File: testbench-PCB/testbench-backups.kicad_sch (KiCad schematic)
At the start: 16 parts, among them J2 AVR-ISP-6, SW1 RESET, U1 ATmega2561-16A, U5 ATmega328P_Xplained_Mini, Y1 X322516MLB4SI

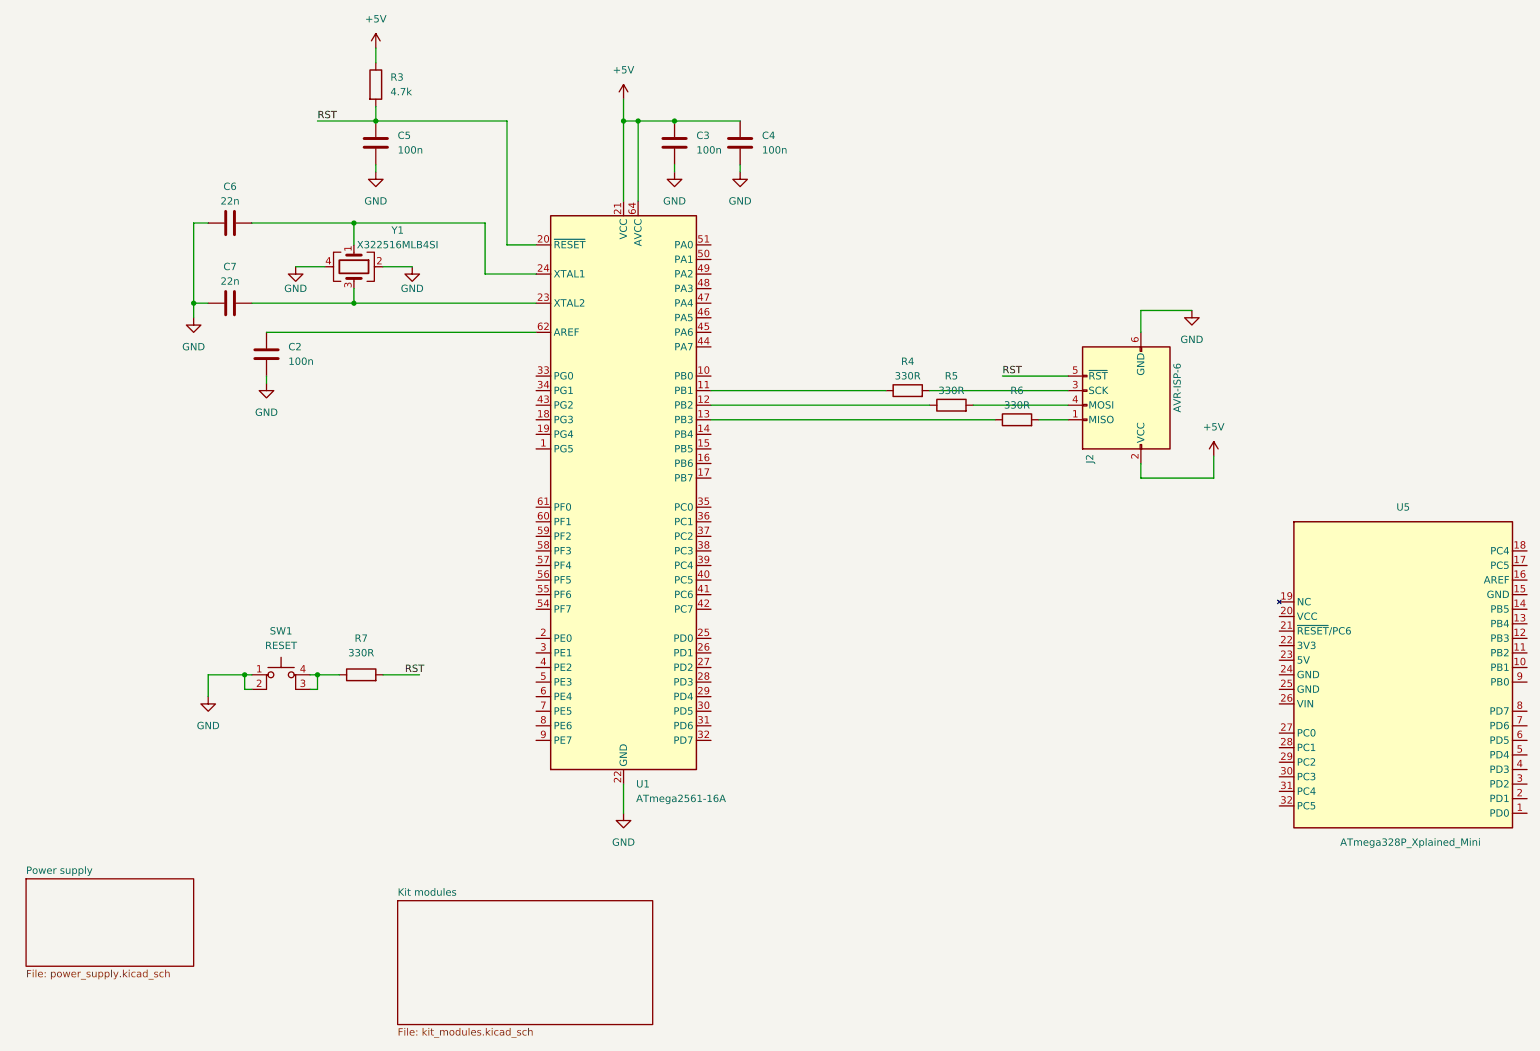
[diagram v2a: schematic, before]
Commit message: Changed USB interface name, MCU moved to separate sheet.
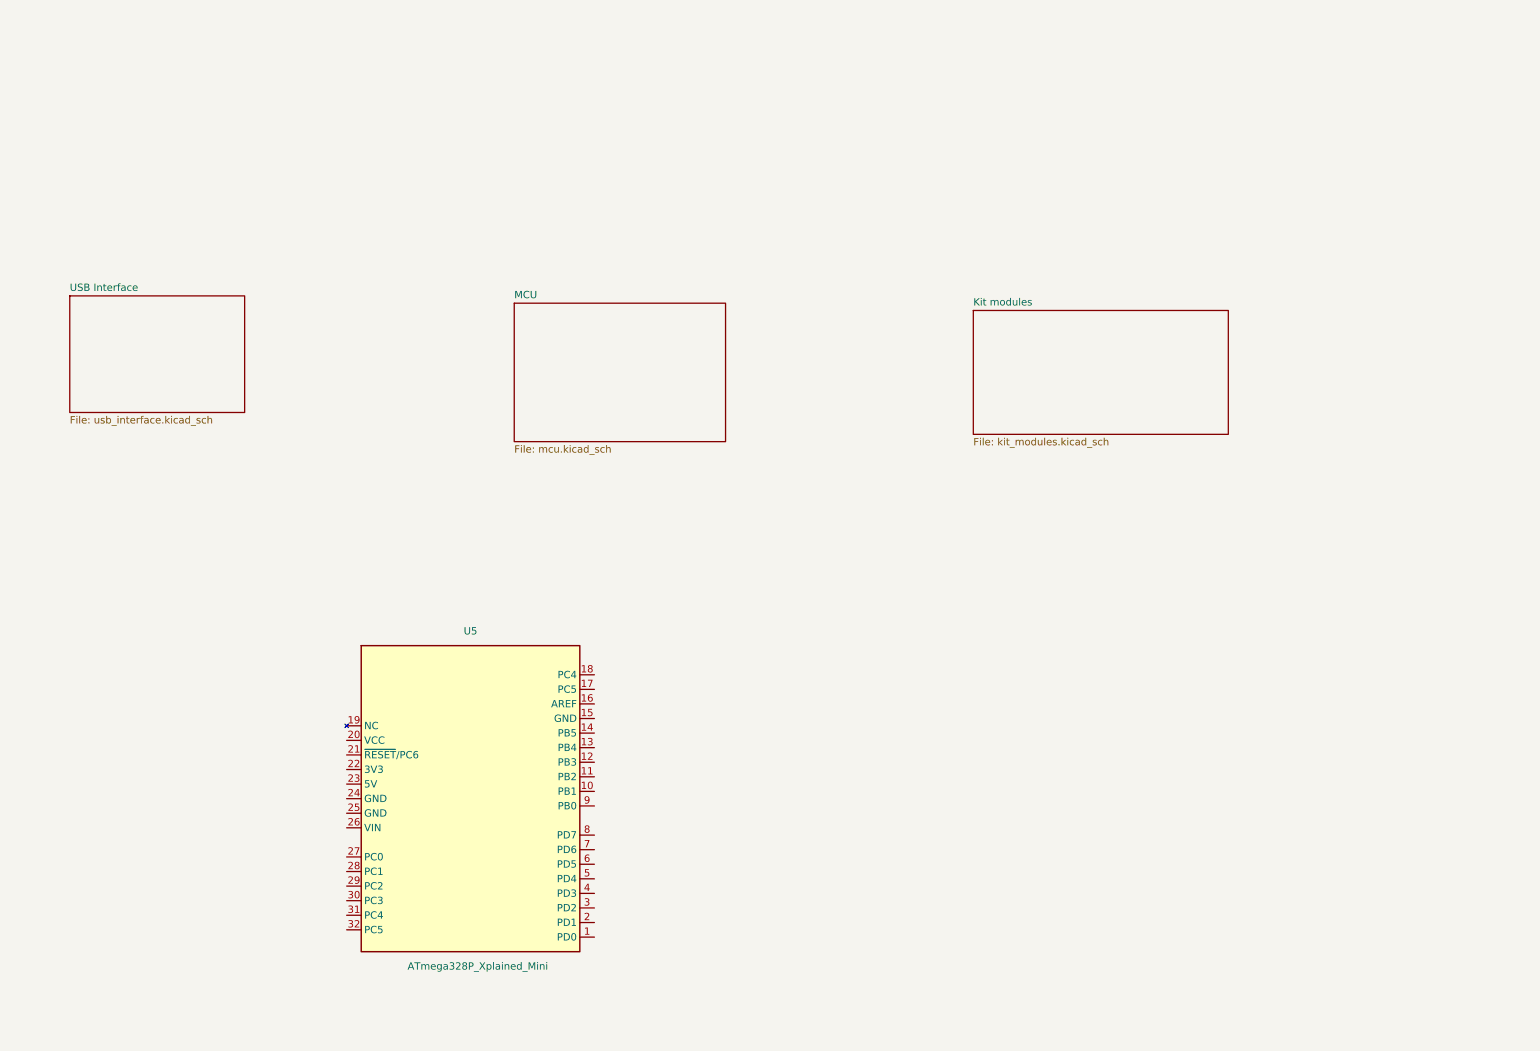
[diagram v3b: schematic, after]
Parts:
- removed C2, C3, C4, C5: 100n, symbol Device:C
- removed C6, C7: 22n, symbol Device:C
- removed J2: AVR-ISP-6, symbol Connector:AVR-ISP-6
- removed R3: 4.7k, symbol Device:R
- removed R4, R5, R6, R7: 330R, symbol Device:R
- removed SW1: RESET, symbol Switch:SW_MEC_5E
- removed U1: ATmega2561-16A, Package_QFP:TQFP-64_14x14mm_P0.8mm, symbol MCU_Microchip_ATmega:ATmega2561-16A
- removed Y1: X322516MLB4SI, symbol Device:Crystal_GND24
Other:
- sheet Power supply renamed USB Interface
- added sheet MCU (mcu.kicad_sch)
- sheet USB Interface: file power_supply.kicad_sch -> usb_interface.kicad_sch
- moved on the sheet: U5
